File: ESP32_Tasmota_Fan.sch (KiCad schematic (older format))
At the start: 19 parts, among them J1 Conn_01x04, J2 Conn_01x06, J6 Conn_01x02_Female, J8 Conn_01x06, U1 mini_esp32

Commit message: Production Version
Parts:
- H1, H2, H3, H4: footprint MountingHole:MountingHole_3.2mm_M3_ISO7380 -> MountingHole:MountingHole_3.2mm_M3_Pad_Via
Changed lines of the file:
@@
 F 0 "H1" H 1550 4646 50  0000 L CNN
 F 1 "MountingHole" H 1550 4555 50  0000 L CNN
-F 2 "MountingHole:MountingHole_3.2mm_M3_ISO7380" H 1450 4600 50  0001 C CNN
+F 2 "MountingHole:MountingHole_3.2mm_M3_Pad_Via" H 1450 4600 50  0001 C CNN
 F 3 "~" H 1450 4600 50  0001 C CNN
 	1    1450 4600
@@
 F 0 "H2" H 1550 4896 50  0000 L CNN
 F 1 "MountingHole" H 1550 4805 50  0000 L CNN
-F 2 "MountingHole:MountingHole_3.2mm_M3_ISO7380" H 1450 4850 50  0001 C CNN
+F 2 "MountingHole:MountingHole_3.2mm_M3_Pad_Via" H 1450 4850 50  0001 C CNN
 F 3 "~" H 1450 4850 50  0001 C CNN
 	1    1450 4850
@@
 F 0 "H3" H 1550 5146 50  0000 L CNN
 F 1 "MountingHole" H 1550 5055 50  0000 L CNN
-F 2 "MountingHole:MountingHole_3.2mm_M3_ISO7380" H 1450 5100 50  0001 C CNN
+F 2 "MountingHole:MountingHole_3.2mm_M3_Pad_Via" H 1450 5100 50  0001 C CNN
 F 3 "~" H 1450 5100 50  0001 C CNN
 	1    1450 5100
@@
 F 0 "H4" H 1550 5396 50  0000 L CNN
 F 1 "MountingHole" H 1550 5305 50  0000 L CNN
-F 2 "MountingHole:MountingHole_3.2mm_M3_ISO7380" H 1450 5350 50  0001 C CNN
+F 2 "MountingHole:MountingHole_3.2mm_M3_Pad_Via" H 1450 5350 50  0001 C CNN
 F 3 "~" H 1450 5350 50  0001 C CNN
 	1    1450 5350

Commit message: Move I2C Pins for BME280
IO34 can only do input, so it is not suitable for I2C
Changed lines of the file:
@@
 Text GLabel 10250 1450 0    50   Input ~ 0
 SDO
+Text GLabel 4450 2250 0    50   Input ~ 0
+SCL
 Text GLabel 4450 4050 0    50   Input ~ 0
-SCL
-Text GLabel 4450 3450 0    50   Input ~ 0
 SDA
 $Comp
@@
 NoConn ~ 4650 2450
 Wire Wire Line
+	4450 2250 4650 2250
+Wire Wire Line
 	4450 4050 4650 4050
-Wire Wire Line
-	4450 3450 4650 3450
 $Comp
 L Device:LED D1

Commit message: First step for new design
split up design into multiples
added voltage regulator available at JLCPCB
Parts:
- removed FAN1, FAN2, FAN3, FAN4: Conn_01x04, Connector:FanPinHeader_1x04_P2.54mm_Vertical, symbol Connector_Generic:Conn_01x04
- removed J1: Conn_01x04, Connector_PinHeader_2.54mm:PinHeader_1x04_P2.54mm_Vertical, symbol Connector_Generic:Conn_01x04
- removed J2, J8: Conn_01x06, Connector_PinHeader_2.54mm:PinHeader_1x06_P2.54mm_Vertical, symbol Connector_Generic:Conn_01x06
- removed R2, R3, R4: 10k, Resistor_SMD:R_0805_2012Metric, symbol Device:R_Small
- removed U1: mini_esp32, ESP32_mini:ESP32_mini, symbol ESP32_mini:mini_esp32
- added U1: DS18B20, Package_TO_SOT_THT:TO-92_Inline, symbol Sensor_Temperature:DS18B20
- R1: value 10k -> 4k7
- renumbered J6 to J1, R5 to R2
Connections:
- net labels removed: IO18, IO19, IO26, IO35, PWM1, PWM2, PWM3, PWM4, SENSE1, SENSE2, SENSE3, SENSE4
- wire segments 57 -> 15
- no-connect marks 2 -> 0
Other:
- note added: "LDO Option\n8,7V Voltagedrop\n500mA Iout\n4,35W Ploss"
- note added: "PSU Requirements\n3.3V @ 500mA"
- note added: "Power Input\n12V 5.5mm/2.1mm Barrel Jack"
- note added: "Temperature Sensor Options\n1-Wire: DS18B20\nI2C: NNN"
- moved on the sheet: D1, H1, H2, H3, H4, J1, R2

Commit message: First layouting
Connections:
- net labels added: SENSE1, SENSE2, SENSE3, SENSE4
- wire segments 15 -> 26
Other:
- moved on the sheet: J1
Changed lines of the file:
@@
 L Connector:Conn_01x02_Female J1
 U 1 1 605C2A51
-P 1050 1450
-F 0 "J1" H 942 1635 50  0000 C CNN
-F 1 "Conn_01x02_Female" H 942 1544 50  0000 C CNN
-F 2 "Connector_BarrelJack:BarrelJack_CUI_PJ-102AH_Horizontal" H 1050 1450 50  0001 C CNN
-F 3 "~" H 1050 1450 50  0001 C CNN
-	1    1050 1450
+P 1050 1900
+F 0 "J1" H 942 2085 50  0000 C CNN
+F 1 "Conn_01x02_Female" H 942 1994 50  0000 C CNN
+F 2 "Connector_BarrelJack:BarrelJack_CUI_PJ-102AH_Horizontal" H 1050 1900 50  0001 C CNN
+F 3 "~" H 1050 1900 50  0001 C CNN
+	1    1050 1900
 	-1   0    0    -1
 $EndComp
@@
 L power:GND #PWR07
 U 1 1 605C41B3
-P 1650 1600
-F 0 "#PWR07" H 1650 1350 50  0001 C CNN
-F 1 "GND" H 1655 1427 50  0000 C CNN
-F 2 "" H 1650 1600 50  0001 C CNN
-F 3 "" H 1650 1600 50  0001 C CNN
-	1    1650 1600
+P 1650 2050
+F 0 "#PWR07" H 1650 1800 50  0001 C CNN
+F 1 "GND" H 1655 1877 50  0000 C CNN
+F 2 "" H 1650 2050 50  0001 C CNN
+F 3 "" H 1650 2050 50  0001 C CNN
+	1    1650 2050
 	1    0    0    -1
 $EndComp
@@
 L power:+12V #PWR06
 U 1 1 605C4698
-P 1650 1350
-F 0 "#PWR06" H 1650 1200 50  0001 C CNN
-F 1 "+12V" H 1665 1523 50  0000 C CNN
-F 2 "" H 1650 1350 50  0001 C CNN
-F 3 "" H 1650 1350 50  0001 C CNN
-	1    1650 1350
-	1    0    0    -1
-$EndComp
-Wire Wire Line
-	1250 1450 1650 1450
-Wire Wire Line
-	1250 1550 1650 1550
-Wire Wire Line
-	1650 1550 1650 1600
+P 1650 1800
+F 0 "#PWR06" H 1650 1650 50  0001 C CNN
+F 1 "+12V" H 1665 1973 50  0000 C CNN
+F 2 "" H 1650 1800 50  0001 C CNN
+F 3 "" H 1650 1800 50  0001 C CNN
+	1    1650 1800
+	1    0    0    -1
+$EndComp
+Wire Wire Line
+	1250 1900 1650 1900
+Wire Wire Line
+	1250 2000 1650 2000
+Wire Wire Line
+	1650 2000 1650 2050
 $Comp
 L power:+3V3 #PWR04
 U 1 1 605D50AD
-P 3350 4550
-F 0 "#PWR04" H 3350 4400 50  0001 C CNN
-F 1 "+3V3" H 3365 4723 50  0000 C CNN
-F 2 "" H 3350 4550 50  0001 C CNN
-F 3 "" H 3350 4550 50  0001 C CNN
-	1    3350 4550
-	1    0    0    -1
-$EndComp
-Wire Wire Line
-	3450 4600 3350 4600
-Wire Wire Line
-	3350 4600 3350 4550
+P 2100 5600
+F 0 "#PWR04" H 2100 5450 50  0001 C CNN
+F 1 "+3V3" H 2115 5773 50  0000 C CNN
+F 2 "" H 2100 5600 50  0001 C CNN
+F 3 "" H 2100 5600 50  0001 C CNN
+	1    2100 5600
+	1    0    0    -1
+$EndComp
+Wire Wire Line
+	2200 5650 2100 5650
+Wire Wire Line
+	2100 5650 2100 5600
 $Comp
 L power:GND #PWR01
 U 1 1 605D671C
-P 2800 4700
-F 0 "#PWR01" H 2800 4450 50  0001 C CNN
-F 1 "GND" H 2805 4527 50  0000 C CNN
-F 2 "" H 2800 4700 50  0001 C CNN
-F 3 "" H 2800 4700 50  0001 C CNN
-	1    2800 4700
-	1    0    0    -1
-$EndComp
-Wire Wire Line
-	2800 4700 3450 4700
-Text GLabel 3450 4800 0    50   Input ~ 0
+P 1550 5750
+F 0 "#PWR01" H 1550 5500 50  0001 C CNN
+F 1 "GND" H 1555 5577 50  0000 C CNN
+F 2 "" H 1550 5750 50  0001 C CNN
+F 3 "" H 1550 5750 50  0001 C CNN
+	1    1550 5750
+	1    0    0    -1
+$EndComp
+Wire Wire Line
+	1550 5750 2200 5750
+Text GLabel 2200 5850 0    50   Input ~ 0
 SCL
-Text GLabel 3450 4900 0    50   Input ~ 0
+Text GLabel 2200 5950 0    50   Input ~ 0
 SDA
-Text GLabel 3400 5000 0    50   Input ~ 0
+Text GLabel 2150 6050 0    50   Input ~ 0
 CSB
-Text GLabel 3400 5100 0    50   Input ~ 0
+Text GLabel 2150 6150 0    50   Input ~ 0
 SDO
 $Comp
@@
 PSU Requirements\n3.3V @ 500mA
 Wire Wire Line
-	1650 1450 1650 1350
-Text Notes 850  850  0    50   ~ 0
+	1650 1900 1650 1800
+Text Notes 850  1400 0    50   ~ 0
 Power Input\n12V 5.5mm/2.1mm Barrel Jack
 Text Notes 1350 4100 0    50   ~ 0
 Temperature Sensor Options\n1-Wire: DS18B20\nI2C: NNN
-Text Notes 2750 1100 0    50   ~ 0
+Text Notes 2850 1450 0    50   ~ 0
 LDO Option\n8,7V Voltagedrop\n500mA Iout\n4,35W Ploss
 $Sheet
-S 2650 2650 1800 950
+S 2150 1650 900  500
 U 6192B19F
 F0 "DC/DC Buck" 50
 F1 "BuckConverter.sch" 50
-$EndSheet
+F2 "VOUT" I R 3050 1900 50
+F3 "VIN" I L 2150 1900 50
+$EndSheet
+Wire Wire Line
+	1650 1900 2150 1900
+Connection ~ 1650 1900
+Wire Wire Line
+	3050 1900 3350 1900
+Wire Wire Line
+	3350 1900 3350 1800
+$Comp
+L power:+3V3 #PWR010
+U 1 1 618AE64B
+P 3350 1800
+F 0 "#PWR010" H 3350 1650 50  0001 C CNN
+F 1 "+3V3" H 3365 1973 50  0000 C CNN
+F 2 "" H 3350 1800 50  0001 C CNN
+F 3 "" H 3350 1800 50  0001 C CNN
+	1    3350 1800
+	1    0    0    -1
+$EndComp
+Text Label 5400 2050 0    50   ~ 0
+SENSE1
+Wire Wire Line
+	5400 2050 5750 2050
+Text Label 5400 2150 0    50   ~ 0
+SENSE2
+Text Label 5400 2250 0    50   ~ 0
+SENSE3
+Text Label 5400 2350 0    50   ~ 0
+SENSE4
+Wire Wire Line
+	5400 2350 5750 2350
+Wire Wire Line
+	5400 2250 5750 2250
+Wire Wire Line
+	5400 2150 5750 2150
+Text Label 8750 2400 0    50   ~ 0
+SENSE3
+Text Label 8750 3000 0    50   ~ 0
+SENSE4
+Wire Wire Line
+	8750 3000 9100 3000
+Wire Wire Line
+	8750 2400 9100 2400
+Wire Wire Line
+	8750 1800 9100 1800
+Text Label 8750 1800 0    50   ~ 0
+SENSE2
+Wire Wire Line
+	8750 1200 9100 1200
+Text Label 8750 1200 0    50   ~ 0
+SENSE1
 $EndSCHEMATC

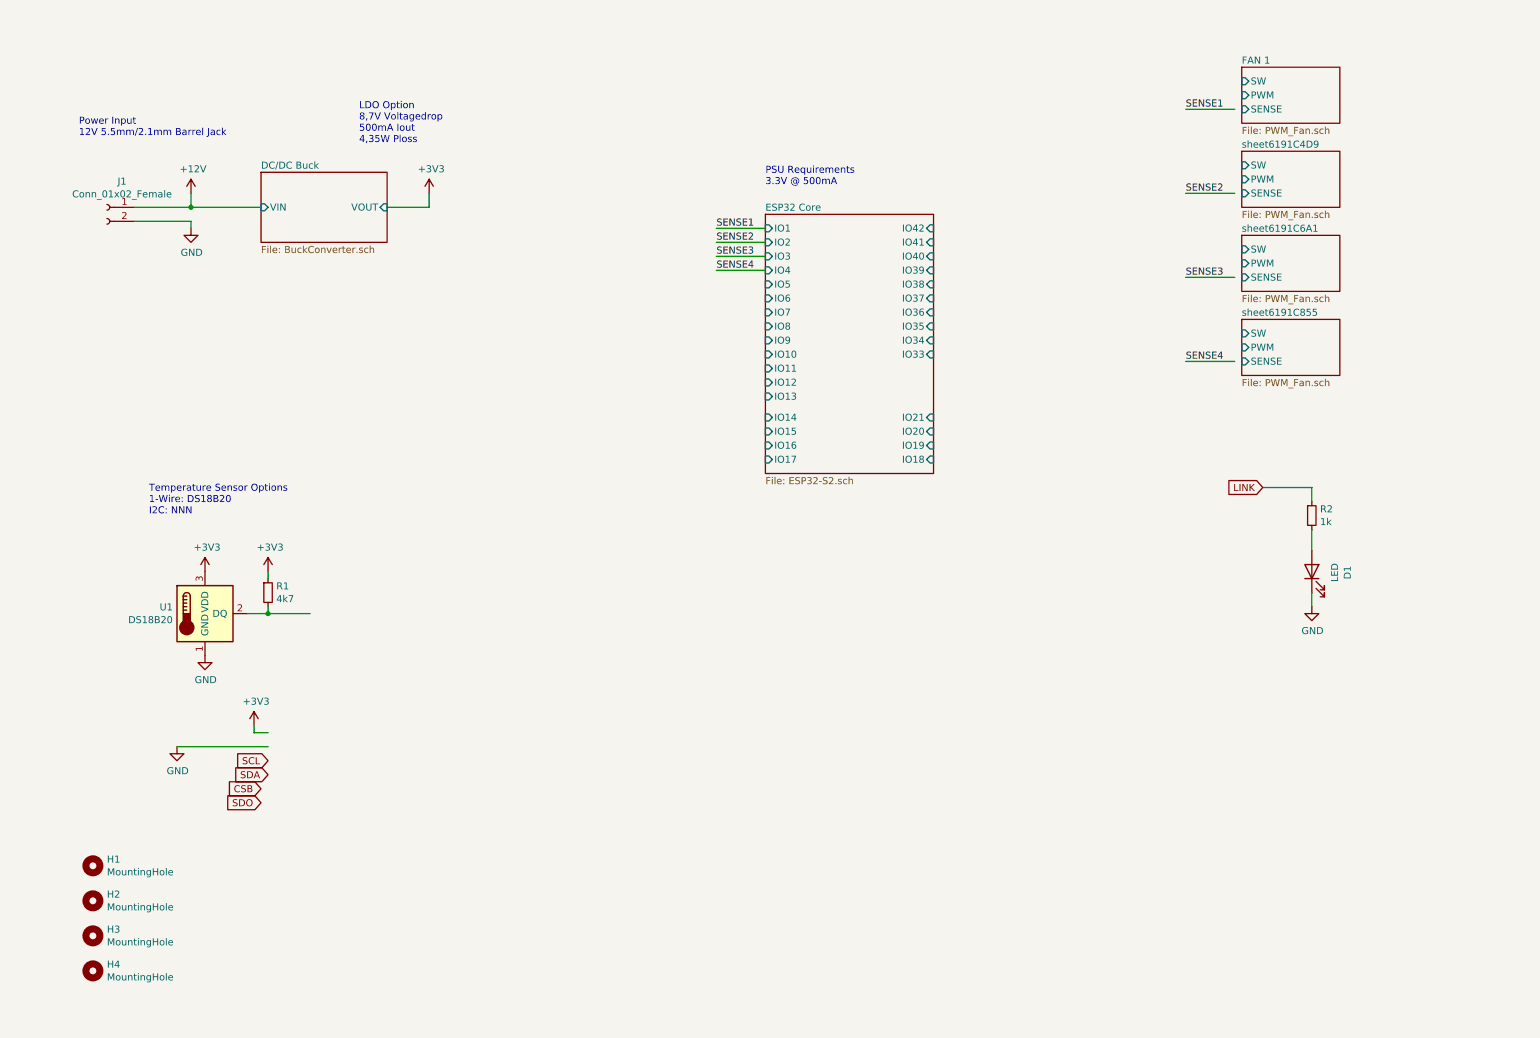
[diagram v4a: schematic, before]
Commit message: First iteration with new ES32 - but not S2
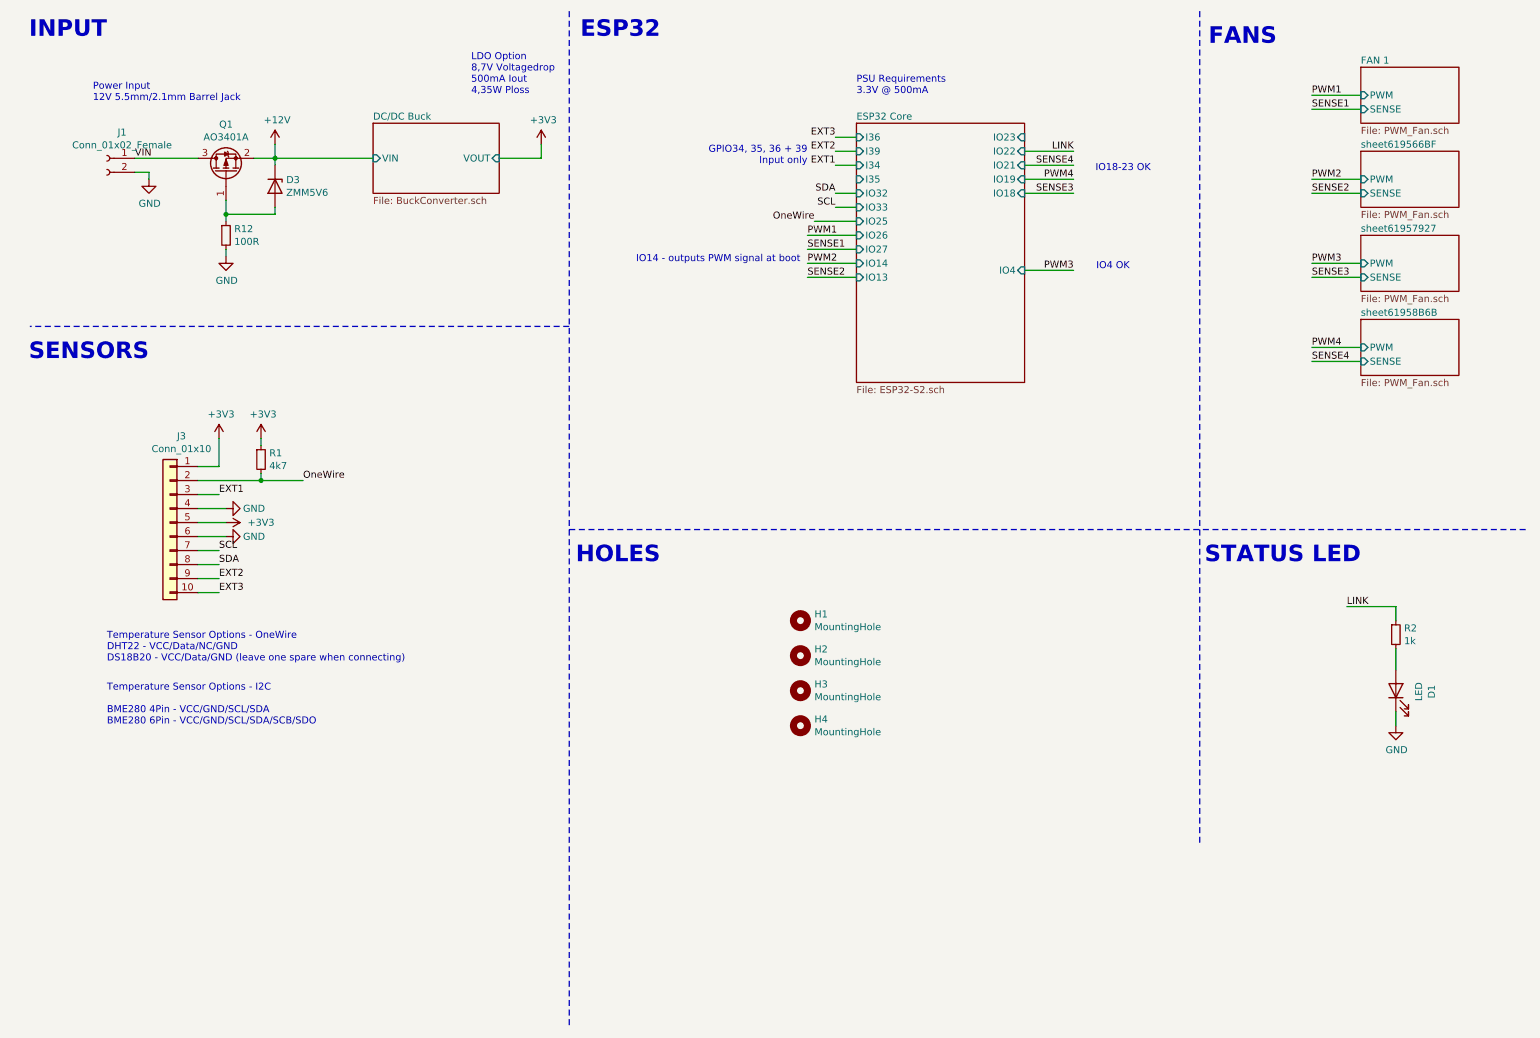
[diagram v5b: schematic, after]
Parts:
- removed U1: DS18B20, Package_TO_SOT_THT:TO-92_Inline, symbol Sensor_Temperature:DS18B20
- added D3: ZMM5V6, Diode_SMD:D_MiniMELF, symbol Device:D_Zener
- added J3: Conn_01x10, Connector_PinSocket_2.54mm:PinSocket_1x10_P2.54mm_Vertical, symbol Connector_Generic:Conn_01x10
- added Q1: AO3401A, Package_TO_SOT_SMD:SOT-23, symbol Transistor_FET:AO3401A
- added R12: 100R, Resistor_SMD:R_0805_2012Metric, symbol Device:R_Small
- D1: footprint LED_THT:LED_D3.0mm -> LED_SMD:LED_0805_2012Metric; LCSC (none) -> C2296
- R1: LCSC (none) -> C17673
- R2: LCSC (none) -> C17513
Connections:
- net labels added: EXT1, EXT2, EXT3, OneWire, PWM1, PWM2, PWM3, PWM4, VIN
- net labels removed: CSB, SDO
- wire segments 26 -> 55
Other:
- note added: "ESP32"
- note added: "FANS"
- note added: "GPIO34, 35, 36 + 39 \nInput only"
- note added: "HOLES"
- note added: "INPUT"
- note added: "IO14 - outputs PWM signal at boot"
- note added: "IO18-23 OK"
- note added: "IO4 OK"
- note added: "SENSORS"
- note added: "STATUS LED"
- note added: "Temperature Sensor Options - I2C\n\nBME280 4Pin - VCC/GND/SCL/SDA\nBME280 6Pin - VCC/GND/SCL/SDA/SCB/SDO"
- note added: "Temperature Sensor Options - OneWire\nDHT22 - VCC/Data/NC/GND\nDS18B20 - VCC/Data/GND (leave one spare when connecting)"
- note removed: "Temperature Sensor Options\n1-Wire: DS18B20\nI2C: NNN"
- moved on the sheet: D1, H1, H2, H3, H4, J1, R1, R2
